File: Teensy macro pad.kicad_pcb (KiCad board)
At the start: 2 copper layers, 79 x 122.4 mm, 44 parts, among them J1 USB_C_Receptacle_USB2.0_14P, J2 AVR-ISP-6, J3 Conn_01x05_Pin, SW0,0 CherryMX, SW0,1 CherryMX, SW0,2 CherryMX, SW0,3 CherryMX, SW0,4 CherryMX, SW1 SW_Push, SW1,0 CherryMX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

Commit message: Add test points for VBUS, XTAL1, and XTAL2
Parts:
- added TP_VBUS1: TestPoint, TestPoint:TestPoint_Pad_D2.0mm, F.Cu at (44.5, 51.5)
- added TP_XTAL1: TestPoint, TestPoint:TestPoint_Pad_D2.0mm, F.Cu at (70.5, 53.0)
- added TP_XTAL2: TestPoint, TestPoint:TestPoint_Pad_D2.0mm, F.Cu at (70.5, 56.0)
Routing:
- net /VBUS: track 22.0 -> 34.0 mm
- net Net-(U1-XTAL2): track 11.1 -> 19.7 mm, vias 2 -> 3
- net Net-(U1-XTAL1): track 12.4 -> 15.9 mm
- net Net-(U1-PD4): track 99.8 -> 101.7 mm
- net Net-(U1-PB4): track 45.0 -> 46.9 mm
- net Net-(U1-PB5): track 26.8 -> 28.7 mm
- net Net-(U1-PD7): track 63.3 -> 65.2 mm
- net Net-(U1-PD6): track 81.5 -> 83.4 mm

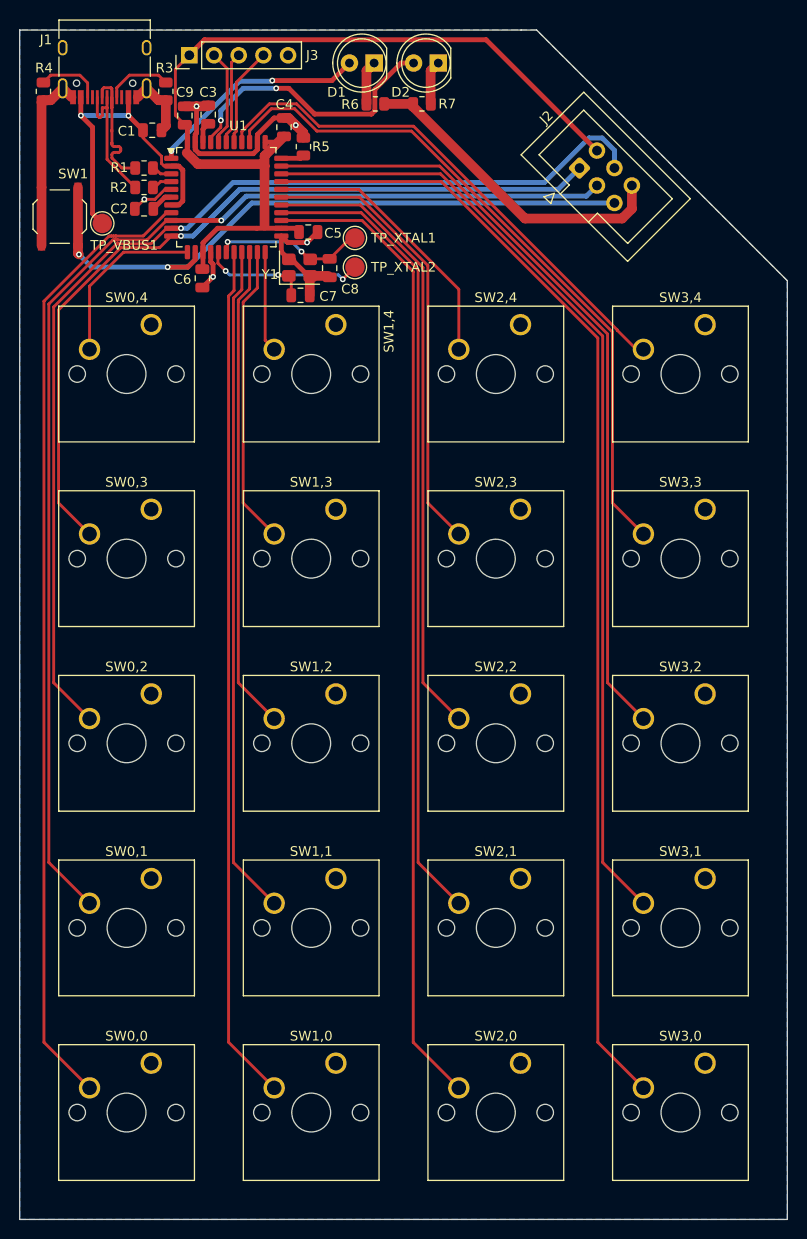
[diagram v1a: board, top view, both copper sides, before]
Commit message: Add holes for bridge pins on the switches
The switches I intend to use for the project have two extra pins in the
bottom corners, which are simply bridged together. Rather than cut them
off, it seems like a good opportunity to try customizing a footprint, so
create a modified footprint which adds holes for the pins. The Cherry MX
datasheet [0] provided pin locations and recommended hole dimensions.

[0]: https://cdn.sparkfun.com/datasheets/Components/Switches/MX%20Series.pdf
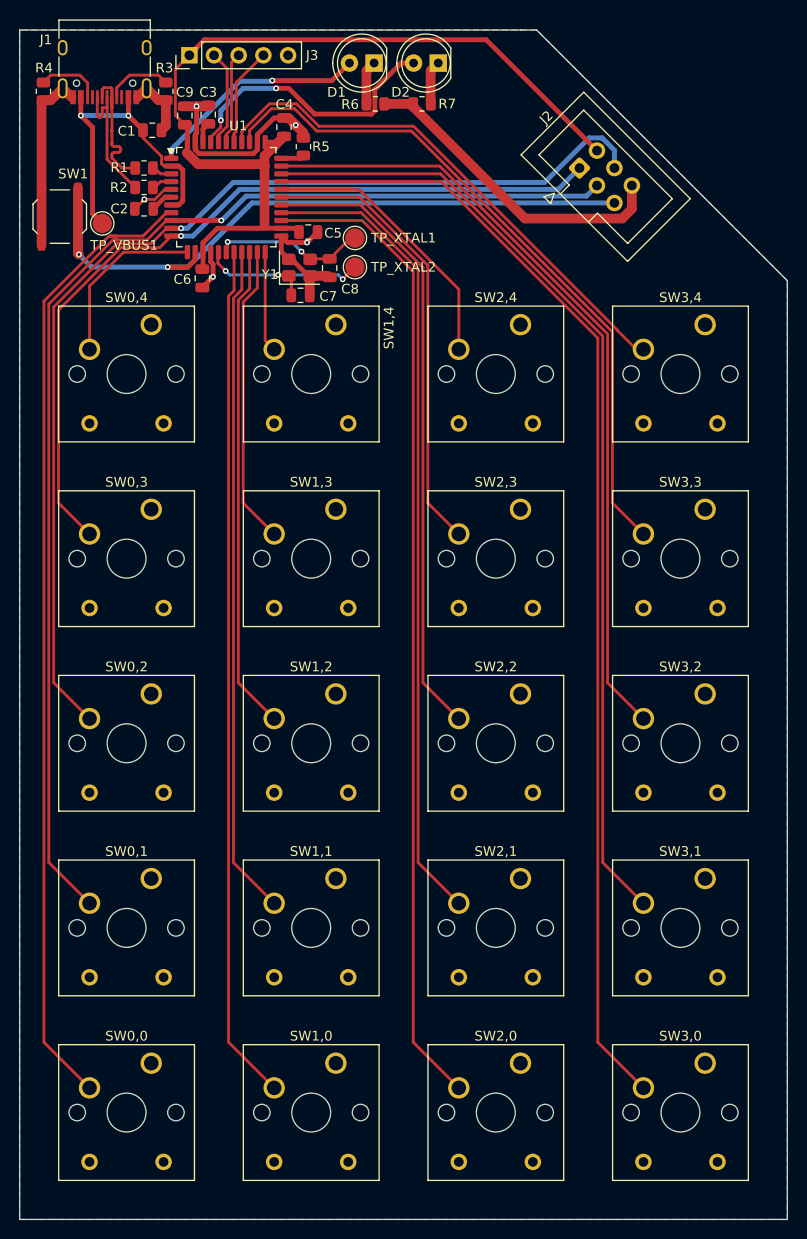
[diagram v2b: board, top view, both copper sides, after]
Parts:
- SW0,0, SW0,1, SW0,2, SW0,3, SW0,4, SW1,0, SW1,1, SW1,2, SW1,3, SW1,4, SW2,0, SW2,1, SW2,2, SW2,3, SW2,4, SW3,0, SW3,1, SW3,2, SW3,3, SW3,4: footprint Button_Switch_Keyboard:SW_Cherry_MX_1.00u_PCB -> CherryMX with bridge:SW_Cherry_MX_1.00u_PCB_with_bridge
